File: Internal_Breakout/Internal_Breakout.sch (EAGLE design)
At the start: 31 parts, among them T1 2N4401, T2 2N4401, U1 MCP10804-T, U2 MIC5205-5V

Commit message: Licenses
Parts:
- added D1: FM4007W, CYCFI_diode:FM4007W
- added H5, H6: (no value), con-lstb:MA03-1_EDITED
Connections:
- new net N$4: C12.1, C6.1, D1.C, U1.OUT, U2.EN, U2.IN
- net 5.4V: now also H5.2, H6.2
- net 9.3V: now also H5.3, H6.3
- net GND: now also H5.1, H6.1
- net VCC: now also D1.A; no longer C12.1, C6.1, U1.OUT, U2.EN, U2.IN
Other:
- note added: "201605"
- note added: "5V"
- note added: "9V"
- note added: "Internal Breakout Project by Cycfi Research is licensed under a Creative Commons Attribution-ShareAlike 4.0 International License. Copyright CYCFI Research Inc. 2013-2016"
- note added: "SUPPLY EXPANSION HEADERS"
- note added: "v1.2"
- note removed: "2015009"
- note removed: "Internal Breakout Project by Cycfi Research is licensed under a Creative Commons Attribution 3.0 Unported License. http://creativecommons.org/licenses/by/3.0/deed.en_US Copyright CYCFI Research Inc. 2013-2015"
- note removed: "v1.1"
- moved on the sheet: C1, C10, C11, C12, C13, C2, C3, C4, C5, C6, C7, C8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

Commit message: *update license date
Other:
- note added: "201718"
- note added: "Internal Breakout Project by Cycfi Research is licensed under a Creative Commons Attribution-ShareAlike 4.0 International License. Copyright CYCFI Research Inc. 2013-2017"
- note removed: "201605"
- note removed: "Internal Breakout Project by Cycfi Research is licensed under a Creative Commons Attribution-ShareAlike 4.0 International License. Copyright CYCFI Research Inc. 2013-2016"
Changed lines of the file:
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@@
 <text x="7.62" y="7.62" size="2.54" layer="95">Internal Breakout Project by Cycfi Research is licensed under a
 Creative Commons Attribution-ShareAlike 4.0 International License.
-Copyright CYCFI Research Inc. 2013-2016</text>
-<text x="200.025" y="11.43" size="2.1844" layer="95">201605</text>
+Copyright CYCFI Research Inc. 2013-2017</text>
+<text x="200.025" y="11.43" size="2.1844" layer="95">201718</text>
 <text x="175.26" y="1.27" size="2.54" layer="94">12/29/2015 2:35:25 PM</text>
 <text x="203.2" y="119.38" size="2.54" layer="95">SUPPLY EXPANSION HEADERS</text>

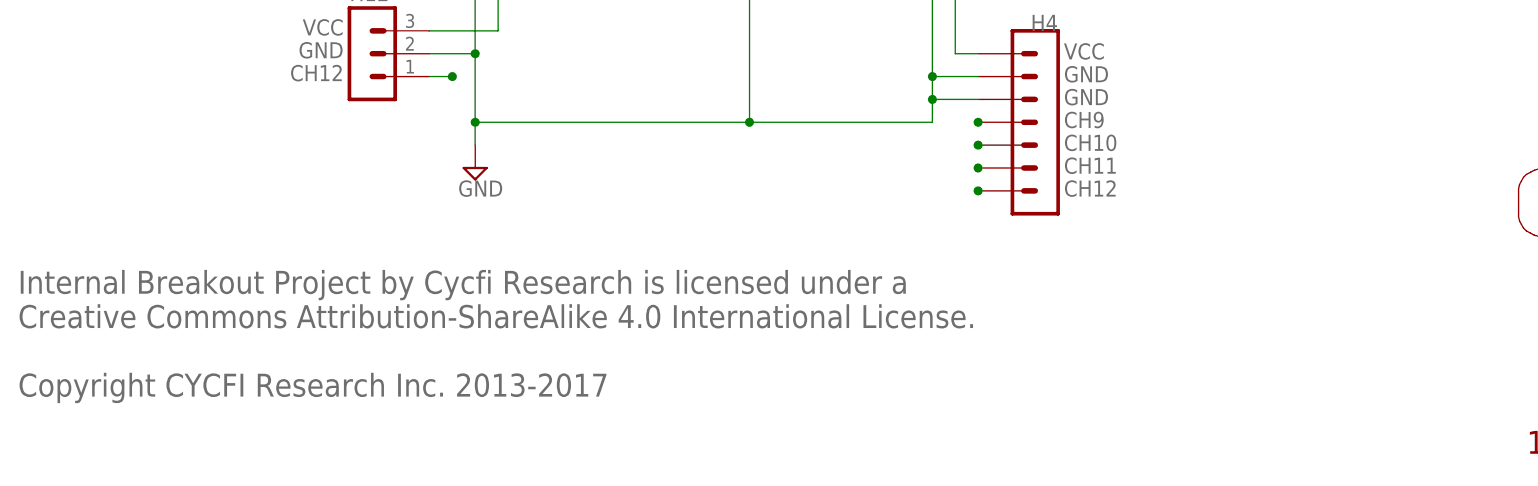
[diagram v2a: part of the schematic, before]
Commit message: Updated Notes "For Nu Project" instead of "Nexus"
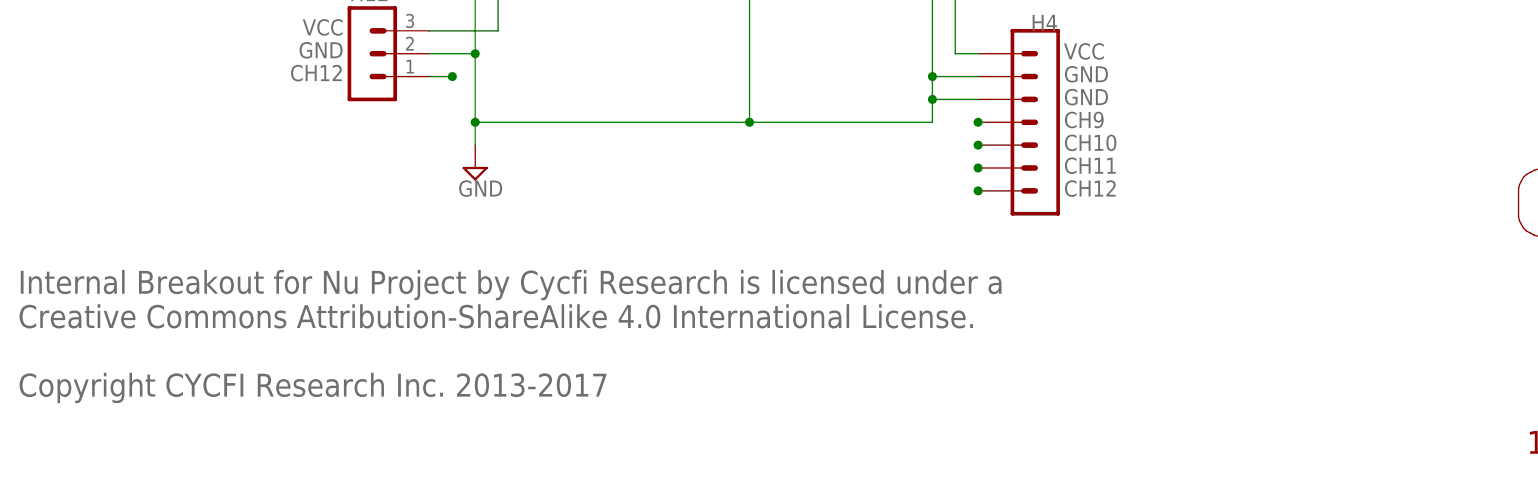
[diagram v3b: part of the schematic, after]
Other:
- note added: "Internal Breakout for Nu Project by Cycfi Research is licensed under a Creative Commons Attribution-ShareAlike 4.0 International License. Copyright CYCFI Research Inc. 2013-2017"
- note removed: "Internal Breakout Project by Cycfi Research is licensed under a Creative Commons Attribution-ShareAlike 4.0 International License. Copyright CYCFI Research Inc. 2013-2017"
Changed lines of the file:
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@@
 <?xml version="1.0" encoding="utf-8"?>
 <!DOCTYPE eagle SYSTEM "eagle.dtd">
-<eagle version="6.3">
+<eagle version="7.6.0">
 <drawing>
 <settings>
@@
 <wire x1="139.7" y1="158.75" x2="138.1125" y2="160.3375" width="0.254" layer="95"/>
 <wire x1="138.1125" y1="160.3375" x2="132.08" y2="160.3375" width="0.254" layer="95"/>
-<text x="7.62" y="7.62" size="2.54" layer="95">Internal Breakout Project by Cycfi Research is licensed under a
+<text x="7.62" y="7.62" size="2.54" layer="95">Internal Breakout for Nu Project by Cycfi Research is licensed under a
 Creative Commons Attribution-ShareAlike 4.0 International License.
 Copyright CYCFI Research Inc. 2013-2017</text>

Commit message: Updated document number.
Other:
- note added: "2017018"
- note removed: "201718"
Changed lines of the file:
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@@
 <wire x1="235.93605625" y1="25.186403125" x2="233.45903125" y2="25.186403125" width="0" layer="94"/>
 <wire x1="233.45903125" y1="25.186403125" x2="233.45903125" y2="33.142509375" width="0" layer="94"/>
-<text x="254" y="6.985" size="2.1844" layer="95">v1.2</text>
+<text x="254" y="6.985" size="2.54" layer="95">v1.2</text>
 <text x="160.02" y="162.56" size="1.778" layer="96">LP2985IM5-6.1/NOPB</text>
 <text x="38.1" y="111.76" size="1.778" layer="95">Note: 1x3 male header
@@
 Creative Commons Attribution-ShareAlike 4.0 International License.
 Copyright CYCFI Research Inc. 2013-2017</text>
-<text x="200.025" y="11.43" size="2.1844" layer="95">201718</text>
+<text x="200.025" y="11.43" size="2.54" layer="95">2017018</text>
 <text x="175.26" y="1.27" size="2.54" layer="94">12/29/2015 2:35:25 PM</text>
 <text x="203.2" y="119.38" size="2.54" layer="95">SUPPLY EXPANSION HEADERS</text>
